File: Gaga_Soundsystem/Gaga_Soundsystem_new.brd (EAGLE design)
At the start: 160 x 100 mm, 15 parts, among them IC1 TUSB2046VF, Q2 6MHZ

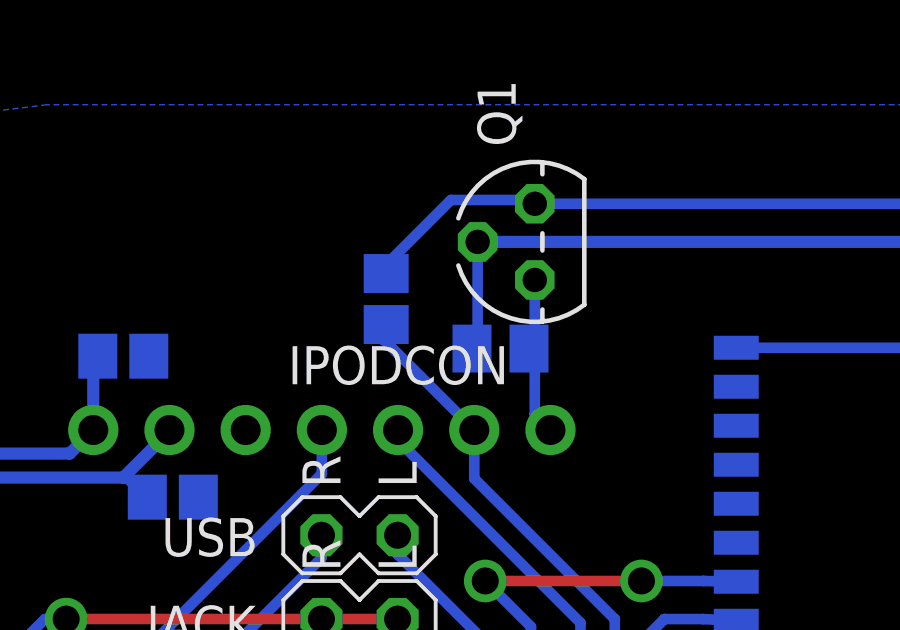
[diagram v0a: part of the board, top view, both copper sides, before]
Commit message: working 8x8 matrix board (tlc4)
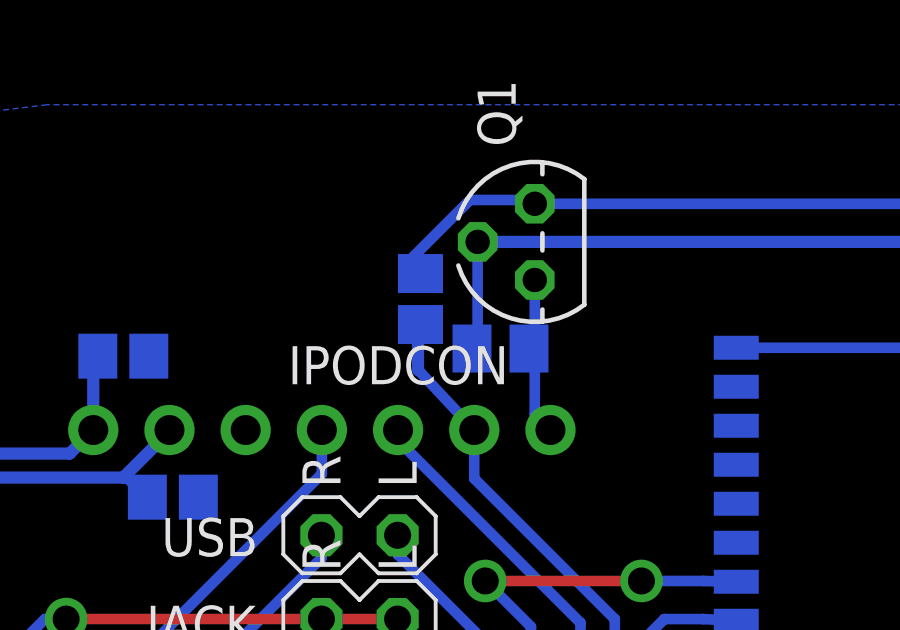
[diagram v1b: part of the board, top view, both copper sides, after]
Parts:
- moved R3 1.14 mm to (98.4, 75.9)
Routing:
- net 5.0V: track 109.0 -> 107.9 mm
- net TX0: track 67.9 -> 67.2 mm
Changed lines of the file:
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@@
 <element name="Q1" library="transistors" package="TO-92" value="" x="102.235" y="77.851" rot="R90"/>
 <element name="R2" library="resistor" package="M0805" value="10K" x="101.092" y="74.295" rot="MR0"/>
-<element name="R3" library="resistor" package="R0805" value="10K" x="97.282" y="75.946" rot="MR270"/>
+<element name="R3" library="resistor" package="R0805" value="10K" x="98.425" y="75.946" rot="MR270"/>
 <element name="IC1" library="jt-texas" package="TQFP32-08" value="TUSB2046VF" x="78.74" y="69.596" rot="MR270"/>
 <element name="Q2" library="crystal" package="HC49/S" value="6MHZ" x="70.739" y="69.342" rot="R90">
@@
 <contactref element="Q1" pad="3"/>
 <contactref element="R3" pad="1"/>
-<wire x1="97.028" y1="76.835" x2="97.282" y2="77.089" width="0.3556" layer="16"/>
-<wire x1="97.282" y1="77.089" x2="99.441" y2="79.248" width="0.3556" layer="16"/>
-<wire x1="99.441" y1="79.248" x2="102.108" y2="79.248" width="0.3556" layer="16"/>
+<wire x1="97.917" y1="77.089" x2="100.076" y2="79.248" width="0.3556" layer="16"/>
+<wire x1="100.076" y1="79.248" x2="102.108" y2="79.248" width="0.3556" layer="16"/>
 <wire x1="102.108" y1="79.248" x2="102.235" y2="79.121" width="0.3556" layer="16"/>
 <wire x1="102.235" y1="79.121" x2="122.809" y2="79.121" width="0.3556" layer="16"/>
@@
 <wire x1="123.825" y1="52.959" x2="113.157" y2="52.959" width="0.3556" layer="16"/>
 <wire x1="113.157" y1="52.959" x2="113.03" y2="53.086" width="0.3556" layer="16"/>
-<wire x1="97.282" y1="76.796" x2="97.282" y2="77.089" width="0.4064" layer="16"/>
+<wire x1="98.425" y1="76.796" x2="97.917" y2="77.089" width="0.4064" layer="16"/>
 </signal>
 <signal name="GND">
@@
 <wire x1="76.151" y1="49.358" x2="73.914" y2="47.121" width="0.3556" layer="16"/>
 <contactref element="R3" pad="2"/>
-<wire x1="96.735" y1="75.057" x2="97.199971875" y2="74.593678125" width="0.3556" layer="16"/>
-<wire x1="97.199971875" y1="74.593678125" x2="98.425" y2="73.373" width="0.3556" layer="16"/>
-<wire x1="98.425" y1="73.373" x2="100.218" y2="71.58" width="0.3556" layer="16"/>
-<wire x1="97.282" y1="75.096" x2="97.199971875" y2="75.096" width="0.4064" layer="16"/>
-<wire x1="97.199971875" y1="75.096" x2="97.199971875" y2="74.593678125" width="0.4064" layer="16"/>
+<wire x1="98.386" y1="73.533" x2="98.342971875" y2="73.577678125" width="0.3556" layer="16"/>
+<wire x1="98.342971875" y1="73.577678125" x2="98.425" y2="73.5" width="0.3556" layer="16"/>
+<wire x1="98.425" y1="73.5" x2="100.218" y2="71.58" width="0.3556" layer="16"/>
+<wire x1="98.425" y1="75.096" x2="98.342971875" y2="74.969" width="0.4064" layer="16"/>
+<wire x1="98.342971875" y1="74.969" x2="98.342971875" y2="73.577678125" width="0.4064" layer="16"/>
 </signal>
 <signal name="IPODR">

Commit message: alt
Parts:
- added IC2: LM358, SparkFun-AnalogIC:DIP08
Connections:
- new net V+: IC2.8
- new net V-: IC2.4
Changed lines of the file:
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@@
 <layer number="151" name="HeatSink" color="7" fill="1" visible="yes" active="yes"/>
 <layer number="152" name="_bDocu" color="7" fill="1" visible="yes" active="yes"/>
+<layer number="199" name="Contour" color="7" fill="1" visible="yes" active="yes"/>
 <layer number="200" name="200bmp" color="1" fill="10" visible="yes" active="yes"/>
 <layer number="201" name="201bmp" color="2" fill="10" visible="yes" active="yes"/>
@@
 <element name="R5" library="resistor" package="R0805" value="15K" x="88.519" y="74.041" rot="MR0"/>
 <element name="R6" library="resistor" package="R0805" value="15K" x="90.17" y="69.342" rot="MR0"/>
+<element name="IC2" library="SparkFun-AnalogIC" package="DIP08" value="LM358" x="19.685" y="8.382">
+<attribute name="PROD_ID" value="IC-09172" x="19.685" y="8.382" size="1.778" layer="27" display="off"/>
+</element>
 </elements>
 <signals>
@@
 <wire x1="122.428" y1="77.851" x2="100.33" y2="77.851" width="0.4064" layer="16"/>
 </signal>
+<signal name="V+">
+<contactref element="IC2" pad="8"/>
+</signal>
+<signal name="V-">
+<contactref element="IC2" pad="4"/>
+</signal>
 </signals>
